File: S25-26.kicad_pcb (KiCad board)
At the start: 6 copper layers, 90 x 90 mm, 0 parts

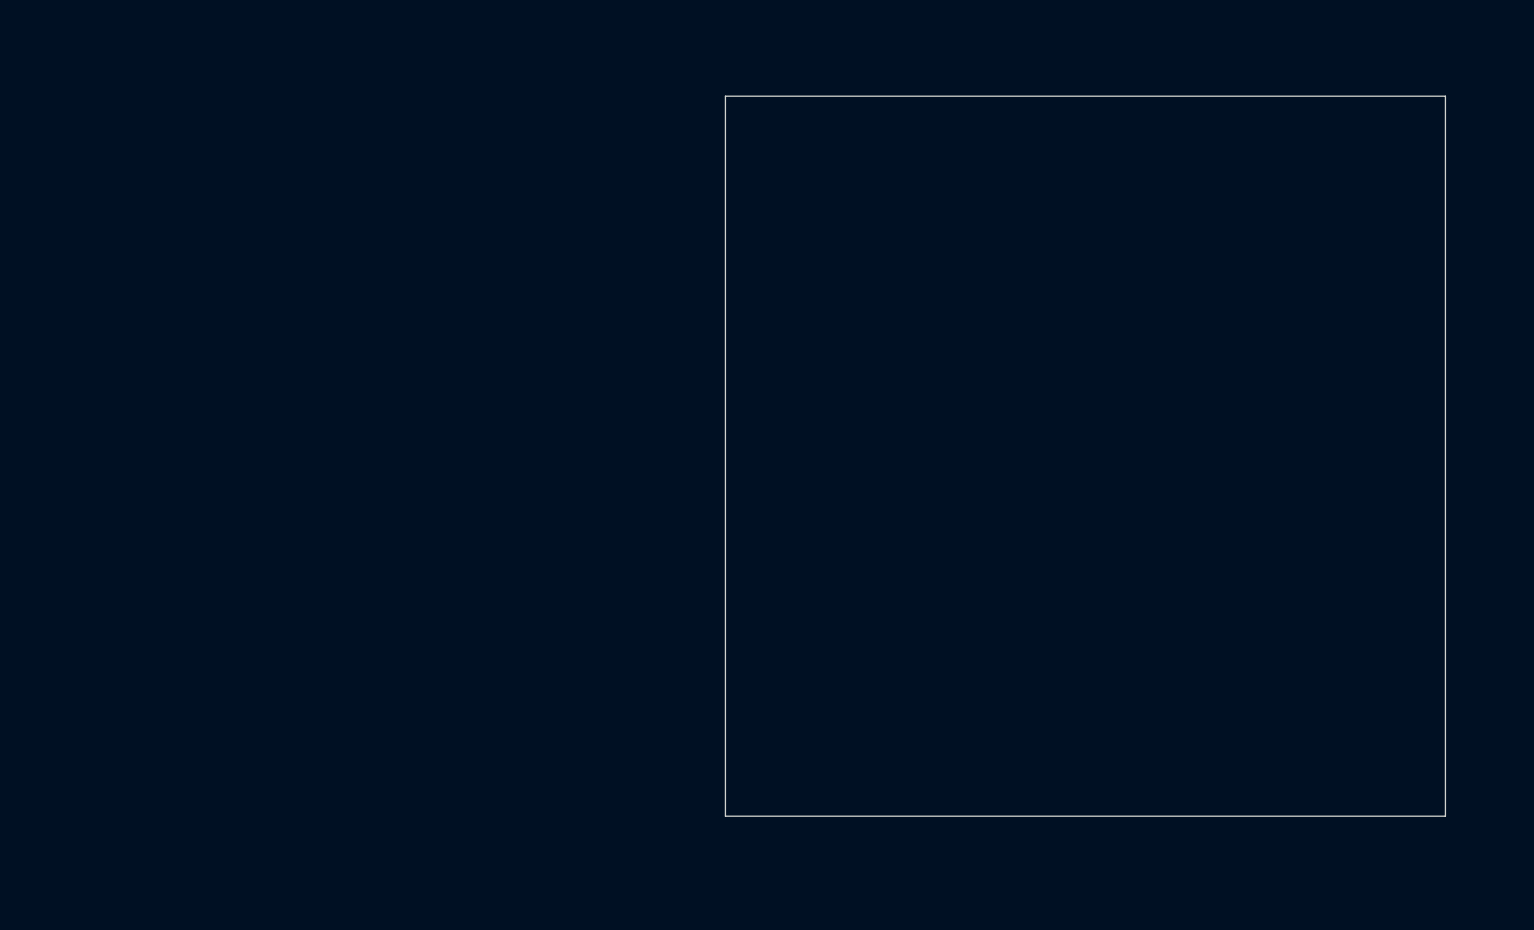
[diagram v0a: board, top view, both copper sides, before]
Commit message: 3v3 Regulator routed; zones for 3v3 and gnd
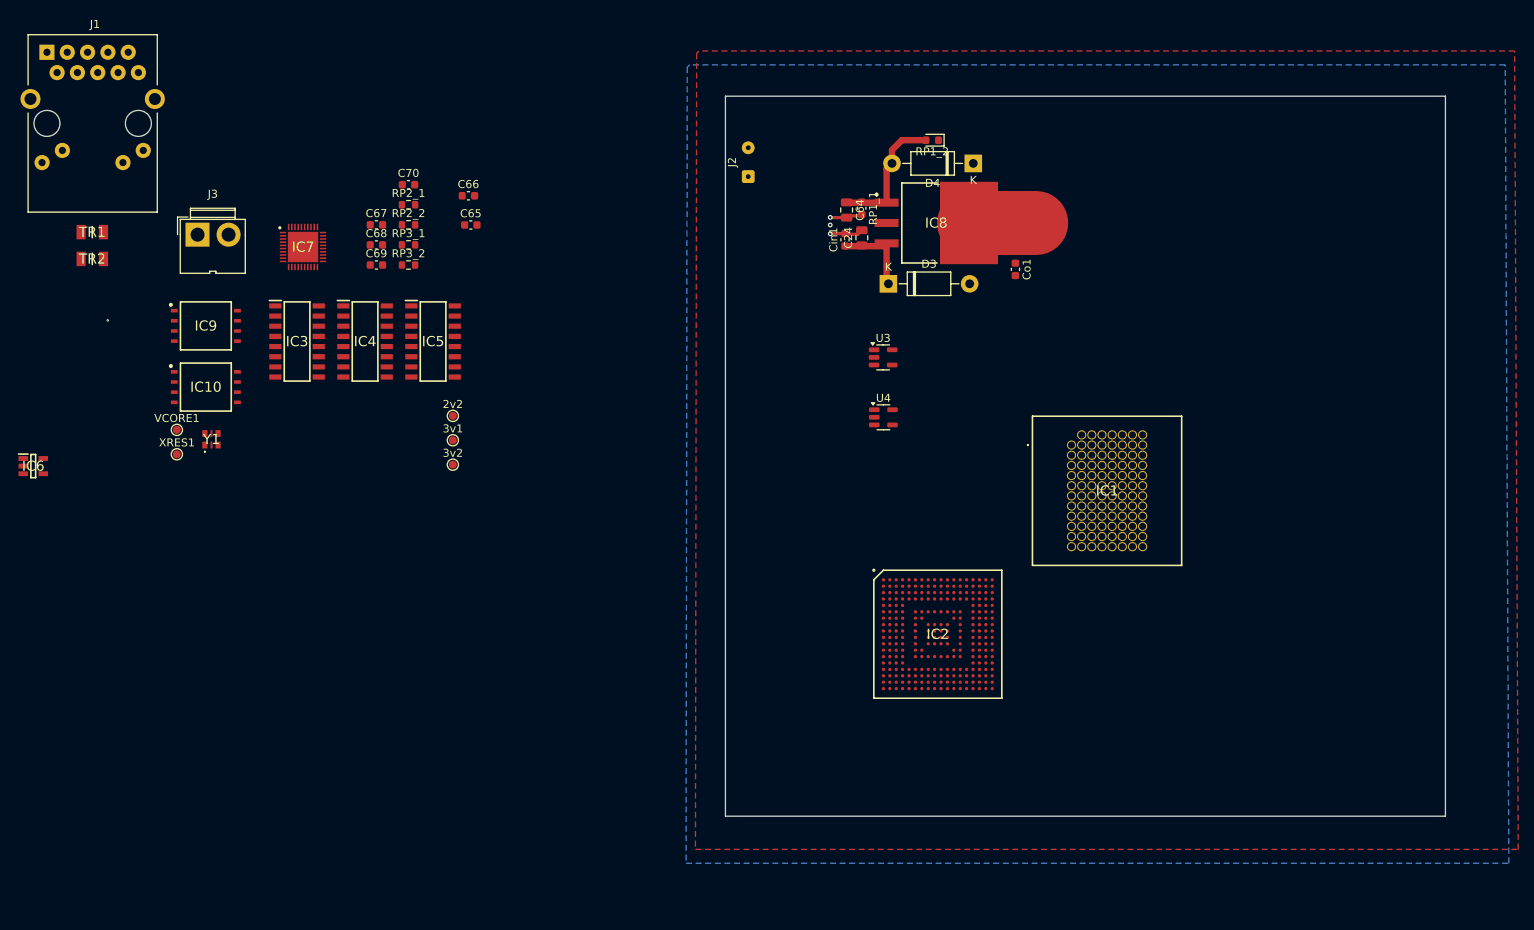
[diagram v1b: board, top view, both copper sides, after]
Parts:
- added 2v2: TestPoint, TestPoint:TestPoint_Pad_D1.0mm, F.Cu at (74.3, 90.2)
- added 3v1: TestPoint, TestPoint:TestPoint_Pad_D1.0mm, F.Cu at (74.3, 93.2)
- added 3v2: TestPoint, TestPoint:TestPoint_Pad_D1.0mm, F.Cu at (74.3, 96.3)
- added C24: 10uF, Capacitor_SMD:C_0805_2012Metric, F.Cu at (125.5, 67.9)
- added C64: 10uF, Capacitor_SMD:C_0805_2012Metric, F.Cu at (123.5, 64.4)
- added C65: 1uF, Capacitor_SMD:C_0603_1608Metric, F.Cu at (76.6, 66.3)
- added C66: 10nF, Capacitor_SMD:C_0603_1608Metric, F.Cu at (76.3, 62.6)
- added C67: 1uF, Capacitor_SMD:C_0603_1608Metric, F.Cu at (64.8, 66.3)
- added C68: 1uF, Capacitor_SMD:C_0603_1608Metric, F.Cu at (64.8, 68.8)
- added C69: 10nF, Capacitor_SMD:C_0603_1608Metric, F.Cu at (64.8, 71.3)
- added C70: 1uF, Capacitor_SMD:C_0603_1608Metric, F.Cu at (68.8, 61.3)
- added Cin1: 1uF, Capacitor_SMD:C_0603_1608Metric, F.Cu at (123.3, 68.2)
- added Co1: 1uF, Capacitor_SMD:C_0603_1608Metric, F.Cu at (144.7, 71.8)
- added D3: 1N4002, Diode_THT:D_DO-41_SOD81_P10.16mm_Horizontal, F.Cu at (128.8, 73.7)
- added D4: 1N4002, Diode_THT:D_DO-41_SOD81_P10.16mm_Horizontal, F.Cu at (139.4, 58.6)
- added IC1: CMV4000-3E5M0PN, SamacSys_Parts:CMV40003E5M0PN, F.Cu at (151.7, 93.8)
- added IC10: MT29F2G01ABAGDWB-IT_G_TR, SamacSys_Parts:SON127P800X600X65-8N, F.Cu at (43.5, 86.6)
- added IC2: XMC7200D-E272K8384AA, SamacSys_Parts:BGA272C80P18X18_1600X1600X170, F.Cu at (134.9, 117.5)
- added IC3: DS90LV048ATM_NOPB, SamacSys_Parts:SOIC127P600X175-16N, F.Cu at (54.9, 80.9)
- added IC4: DS90LV048ATM_NOPB, SamacSys_Parts:SOIC127P600X175-16N, F.Cu at (63.4, 80.9)
- added IC5: DS90LV048ATM_NOPB, SamacSys_Parts:SOIC127P600X175-16N, F.Cu at (71.9, 80.9)
- added IC6: DS90LV011AHMF_NOPB, SamacSys_Parts:SOT95P280X145-5N, F.Cu at (21.9, 96.4)
- added IC7: MXL86110I-AQB-R, SamacSys_Parts:QFN40P500X500X95-41N-D, F.Cu at (55.6, 69.0)
- added IC8: NCV317BD2TR4G, SamacSys_Parts:TO254P1420X457-4N, F.Cu at (134.8, 66.0)
- added IC9: MT29F2G01ABAGDWB-IT_G_TR, SamacSys_Parts:SON127P800X600X65-8N, F.Cu at (43.5, 78.9)
- added J1: RJ45_RB1-125B8G1A, Connector_RJ:RJ45_UDE_RB1-125B8G1A, F.Cu at (23.6, 44.7)
- added J2: DC_IN_PADS, Connector_Wire:SolderWire-0.1sqmm_1x02_P3.6mm_D0.4mm_OD1mm, F.Cu at (111.2, 60.2)
- added J3: Conn_01x02_Pin, Connector:JWT_A3963_1x02_P3.96mm_Vertical, F.Cu at (42.4, 67.5)
- added RP1_1: 164, Capacitor_SMD:C_0603_1608Metric, F.Cu at (125.5, 64.2)
- added RP1_2: 100, Diode_SMD:D_0603_1608Metric, F.Cu at (134.2, 55.7)
- added RP2_1: 100, Resistor_SMD:R_0603_1608Metric, F.Cu at (68.8, 63.8)
- added RP2_2: 150, Resistor_SMD:R_0603_1608Metric, F.Cu at (68.8, 66.3)
- added RP3_1: 120, Resistor_SMD:R_0603_1608Metric, F.Cu at (68.8, 68.8)
- added RP3_2: 90, Resistor_SMD:R_0603_1608Metric, F.Cu at (68.8, 71.3)
- added TR1: PTS120601B1K00P100, SamacSys_Parts:RESC3016X65N, F.Cu at (29.3, 67.2)
- added TR2: PTS120601B1K00P100, SamacSys_Parts:RESC3016X65N, F.Cu at (29.3, 70.5)
- added U3: TPS73601DBV, Package_TO_SOT_SMD:SOT-23-5, F.Cu at (128.1, 82.8)
- added U4: TPS73601DBV, Package_TO_SOT_SMD:SOT-23-5, F.Cu at (128.2, 90.3)
- added VCORE1: TestPoint, TestPoint:TestPoint_Pad_D1.0mm, F.Cu at (39.8, 91.9)
- added XRES1: TestPoint, TestPoint:TestPoint_Pad_D1.0mm, F.Cu at (39.8, 95.0)
- added Y1: DSC1101DM2-012.0000, SamacSys_Parts:DSC1101DM20120000, F.Cu at (44.2, 93.1)
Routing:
- net Net-(D4-A): track 0.00 -> 16.6 mm
- net /Voltage Regulation/DC_LINE_IN_28V: track 0.00 -> 11.0 mm
- net +3V3: track 0.00 -> 8.40 mm
- net GND: track 0.00 -> 8.32 mm, vias 0 -> 3
- net (no net): vias 0 -> 1
- added copper zone on F.Cu, net +3V3
- added copper zone on B.Cu, net GND
- added copper zone on In1.Cu, net GND
- added copper zone on In3.Cu, net GND

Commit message: Ethernet Transceiver
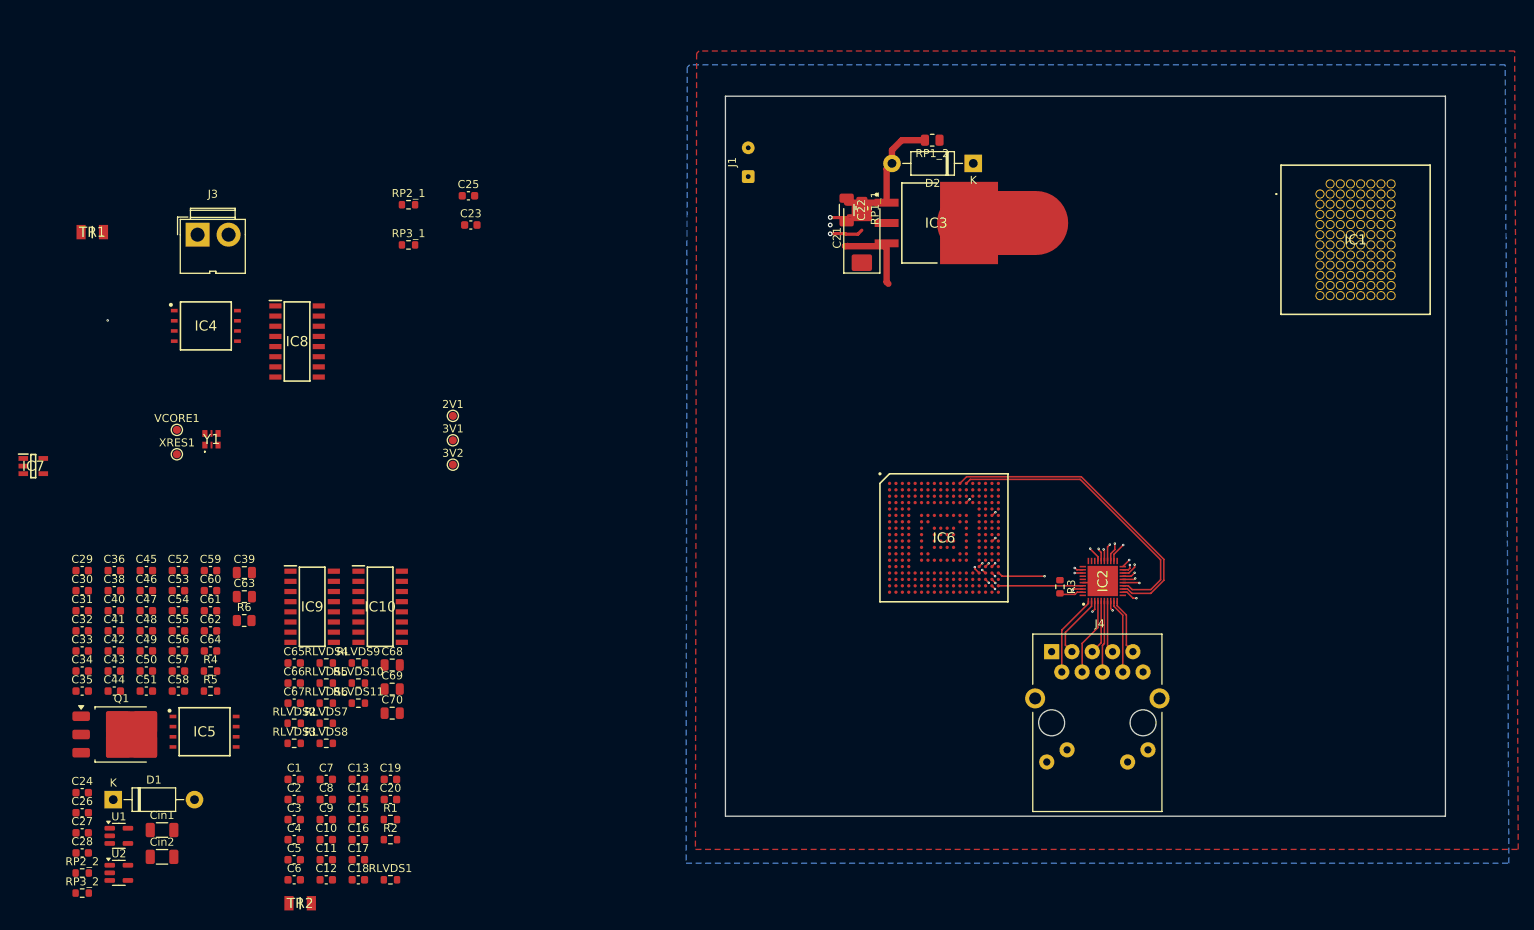
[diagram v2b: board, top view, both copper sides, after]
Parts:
- removed Co1: 1uF, Capacitor_SMD:C_0603_1608Metric
- removed D3: 1N4002, Diode_THT:D_DO-41_SOD81_P10.16mm_Horizontal
- removed the IC4 at (63.4, 80.9)
- removed U3, U4: TPS73601DBV, Package_TO_SOT_SMD:SOT-23-5
- added C1: 0.1uF, Capacitor_SMD:C_0603_1608Metric, F.Cu at (54.5, 135.6)
- added C10: 0.1uF, Capacitor_SMD:C_0603_1608Metric, F.Cu at (58.5, 143.1)
- added C11: 0.1uF, Capacitor_SMD:C_0603_1608Metric, F.Cu at (58.5, 145.6)
- added C12: 0.1uF, Capacitor_SMD:C_0603_1608Metric, F.Cu at (58.5, 148.2)
- added C13: 0.1uF, Capacitor_SMD:C_0603_1608Metric, F.Cu at (62.5, 135.6)
- added C14: 0.1uF, Capacitor_SMD:C_0603_1608Metric, F.Cu at (62.5, 138.1)
- added C15: 0.1uF, Capacitor_SMD:C_0603_1608Metric, F.Cu at (62.5, 140.6)
- added C16: 0.1uF, Capacitor_SMD:C_0603_1608Metric, F.Cu at (62.5, 143.1)
- added C17: 0.1uF, Capacitor_SMD:C_0603_1608Metric, F.Cu at (62.5, 145.6)
- added C18: 0.1uF, Capacitor_SMD:C_0603_1608Metric, F.Cu at (62.5, 148.2)
- added C19: 0.1uF, Capacitor_SMD:C_0603_1608Metric, F.Cu at (66.5, 135.6)
- added C2: 0.1uF, Capacitor_SMD:C_0603_1608Metric, F.Cu at (54.5, 138.1)
- added C20: 0.1uF, Capacitor_SMD:C_0603_1608Metric, F.Cu at (66.5, 138.1)
- added C24: 1uF, Capacitor_SMD:C_0603_1608Metric, F.Cu at (28.0, 137.3)
- added C26: 10nF, Capacitor_SMD:C_0603_1608Metric, F.Cu at (28.0, 139.8)
- added C27: 1uF, Capacitor_SMD:C_0603_1608Metric, F.Cu at (28.0, 142.3)
- added C28: 1uF, Capacitor_SMD:C_0603_1608Metric, F.Cu at (28.0, 144.8)
- added C29: 10uF, Capacitor_SMD:C_0603_1608Metric, F.Cu at (28.0, 109.5)
- added C3: 0.1uF, Capacitor_SMD:C_0603_1608Metric, F.Cu at (54.5, 140.6)
- added C30: 1uF, Capacitor_SMD:C_0603_1608Metric, F.Cu at (28.0, 112.0)
- added C31: 0.1uF, Capacitor_SMD:C_0603_1608Metric, F.Cu at (28.0, 114.5)
- added C32: 0.1uF, Capacitor_SMD:C_0603_1608Metric, F.Cu at (28.0, 117.0)
- added C33: 0.1uF, Capacitor_SMD:C_0603_1608Metric, F.Cu at (28.0, 119.5)
- added C34: 0.1uF, Capacitor_SMD:C_0603_1608Metric, F.Cu at (28.0, 122.0)
- added C35: 0.1uF, Capacitor_SMD:C_0603_1608Metric, F.Cu at (28.0, 124.6)
- added C36: 0.1uF, Capacitor_SMD:C_0603_1608Metric, F.Cu at (32.0, 109.5)
- added C38: 0.1uF, Capacitor_SMD:C_0603_1608Metric, F.Cu at (32.0, 112.0)
- added C39: 0.1uF, Capacitor_SMD:C_0805_2012Metric, F.Cu at (48.3, 109.8)
- added C4: 0.1uF, Capacitor_SMD:C_0603_1608Metric, F.Cu at (54.5, 143.1)
- added C40: 1uF, Capacitor_SMD:C_0603_1608Metric, F.Cu at (32.0, 114.5)
- added C41: 0.1uF, Capacitor_SMD:C_0603_1608Metric, F.Cu at (32.0, 117.0)
- added C42: 0.1uF, Capacitor_SMD:C_0603_1608Metric, F.Cu at (32.0, 119.5)
- added C43: 0.1uF, Capacitor_SMD:C_0603_1608Metric, F.Cu at (32.0, 122.0)
- added C44: 0.1uF, Capacitor_SMD:C_0603_1608Metric, F.Cu at (32.0, 124.6)
- added C45: 0.1uF, Capacitor_SMD:C_0603_1608Metric, F.Cu at (36.0, 109.5)
- added C46: 0.1uF, Capacitor_SMD:C_0603_1608Metric, F.Cu at (36.0, 112.0)
- added C47: 1uF, Capacitor_SMD:C_0603_1608Metric, F.Cu at (36.0, 114.5)
- added C48: 1uF, Capacitor_SMD:C_0603_1608Metric, F.Cu at (36.0, 117.0)
- added C49: 0.1uF, Capacitor_SMD:C_0603_1608Metric, F.Cu at (36.0, 119.5)
- added C5: 0.1uF, Capacitor_SMD:C_0603_1608Metric, F.Cu at (54.5, 145.6)
- added C50: 0.1uF, Capacitor_SMD:C_0603_1608Metric, F.Cu at (36.0, 122.0)
- added C51: 0.1uF, Capacitor_SMD:C_0603_1608Metric, F.Cu at (36.0, 124.6)
- added C52: 10nF, Capacitor_SMD:C_0603_1608Metric, F.Cu at (40.0, 109.5)
- added C53: 0.1uF, Capacitor_SMD:C_0603_1608Metric, F.Cu at (40.0, 112.0)
- added C54: 0.1uF, Capacitor_SMD:C_0603_1608Metric, F.Cu at (40.0, 114.5)
- added C55: 1uF, Capacitor_SMD:C_0603_1608Metric, F.Cu at (40.0, 117.0)
- added C56: 0.1uF, Capacitor_SMD:C_0603_1608Metric, F.Cu at (40.0, 119.5)
- added C57: 2.2uF, Capacitor_SMD:C_0603_1608Metric, F.Cu at (40.0, 122.0)
- added C58: 10nF, Capacitor_SMD:C_0603_1608Metric, F.Cu at (40.0, 124.6)
- added C59: 0.1uF, Capacitor_SMD:C_0603_1608Metric, F.Cu at (44.0, 109.5)
- added C6: 0.1uF, Capacitor_SMD:C_0603_1608Metric, F.Cu at (54.5, 148.2)
- added C60: 2.2uF, Capacitor_SMD:C_0603_1608Metric, F.Cu at (44.0, 112.0)
- added C61: 0.1uF, Capacitor_SMD:C_0603_1608Metric, F.Cu at (44.0, 114.5)
- added C62: 10uF, Capacitor_SMD:C_0603_1608Metric, F.Cu at (44.0, 117.0)
- added C63: 0.1uF, Capacitor_SMD:C_0805_2012Metric, F.Cu at (48.3, 112.8)
- added C64: 1nF, Capacitor_SMD:C_0603_1608Metric, F.Cu at (44.0, 119.5)
- added C65: 1nF, Capacitor_SMD:C_0603_1608Metric, F.Cu at (54.5, 121.0)
- added C66: 1nF, Capacitor_SMD:C_0603_1608Metric, F.Cu at (54.5, 123.6)
- added C7: 0.1uF, Capacitor_SMD:C_0603_1608Metric, F.Cu at (58.5, 135.6)
- added C8: 0.1uF, Capacitor_SMD:C_0603_1608Metric, F.Cu at (58.5, 138.1)
- added C9: 0.1uF, Capacitor_SMD:C_0603_1608Metric, F.Cu at (58.5, 140.6)
- added Cin2: 1uF, Capacitor_SMD:C_1206_3216Metric, F.Cu at (38.0, 145.3)
- added D1: 1N4002, Diode_THT:D_DO-41_SOD81_P10.16mm_Horizontal, F.Cu at (31.9, 138.1)
- added IC9: DS90LV048ATM_NOPB, SamacSys_Parts:SOIC127P600X175-16N, F.Cu at (56.7, 114.0)
- added Q1: ZXT849K, Package_TO_SOT_SMD:TO-252-3_TabPin4, F.Cu at (32.9, 130.0)
- added R1: 1k, Resistor_SMD:R_0603_1608Metric, F.Cu at (66.5, 140.6)
- added R2: 1k, Resistor_SMD:R_0603_1608Metric, F.Cu at (66.5, 143.1)
- added R3: 2.49k, Resistor_SMD:R_0603_1608Metric, F.Cu at (150.2, 111.5)
- added R4: 10k, Resistor_SMD:R_0603_1608Metric, F.Cu at (44.0, 122.0)
- added R5: 10k, Resistor_SMD:R_0603_1608Metric, F.Cu at (44.0, 124.6)
- added R6: 0.1, Resistor_SMD:R_0805_2012Metric, F.Cu at (48.2, 115.7)
- added RLVDS1: 100, Resistor_SMD:R_0603_1608Metric, F.Cu at (66.5, 148.2)
- added RLVDS10: 100, Resistor_SMD:R_0603_1608Metric, F.Cu at (62.5, 123.6)
- added RLVDS11: 100, Resistor_SMD:R_0603_1608Metric, F.Cu at (62.5, 126.1)
- added RLVDS2: 100, Resistor_SMD:R_0603_1608Metric, F.Cu at (54.5, 128.6)
- added RLVDS3: 100, Resistor_SMD:R_0603_1608Metric, F.Cu at (54.5, 131.1)
- added RLVDS4: 100, Resistor_SMD:R_0603_1608Metric, F.Cu at (58.5, 121.0)
- added RLVDS5: 100, Resistor_SMD:R_0603_1608Metric, F.Cu at (58.5, 123.6)
- added RLVDS6: 100, Resistor_SMD:R_0603_1608Metric, F.Cu at (58.5, 126.1)
- added RLVDS7: 100, Resistor_SMD:R_0603_1608Metric, F.Cu at (58.5, 128.6)
- added RLVDS8: 100, Resistor_SMD:R_0603_1608Metric, F.Cu at (58.5, 131.1)
- added RLVDS9: 100, Resistor_SMD:R_0603_1608Metric, F.Cu at (62.5, 121.0)
- added U1: TPS73601MDRBREP, Package_TO_SOT_SMD:SOT-23-5, F.Cu at (32.6, 142.7)
- added U2: TPS73601MDRBREP, Package_TO_SOT_SMD:SOT-23-5, F.Cu at (32.6, 147.3)
- C21: renamed from C24; footprint Capacitor_SMD:C_0805_2012Metric -> Capacitor_Tantalum_SMD:CP_EIA-7343-31_Kemet-D
- C22: renamed from C64; footprint Capacitor_SMD:C_0805_2012Metric -> Capacitor_SMD:C_1206_3216Metric
- C67: value 1uF -> 1nF
- C68, C70: value 1uF -> 0.1uF; footprint Capacitor_SMD:C_0603_1608Metric -> Capacitor_SMD:C_0805_2012Metric
- C69: value 10nF -> 0.1uF; footprint Capacitor_SMD:C_0603_1608Metric -> Capacitor_SMD:C_0805_2012Metric
- Cin1: footprint Capacitor_SMD:C_0603_1608Metric -> Capacitor_SMD:C_1206_3216Metric
- IC10: value MT29F2G01ABAGDWB-IT_G_TR -> DS90LV048ATM_NOPB; footprint SamacSys_Parts:SON127P800X600X65-8N -> SamacSys_Parts:SOIC127P600X175-16N
- IC5: value DS90LV048ATM_NOPB -> MT29F2G01ABAGDWB-IT_G_TR; footprint SamacSys_Parts:SOIC127P600X175-16N -> SamacSys_Parts:SON127P800X600X65-8N
- RP1_1: value 164 -> 165; footprint Capacitor_SMD:C_0603_1608Metric -> Resistor_SMD:R_0805_2012Metric
- RP1_2: footprint Diode_SMD:D_0603_1608Metric -> Resistor_SMD:R_0805_2012Metric
- RP2_1: value 100 -> 46.4k
- RP2_2: value 150 -> 30.9k
- RP3_1: value 120 -> 31.6k
- RP3_2: value 90 -> 42.2k
- moved J4 146.2 mm to (149.2, 119.6)
- moved Cin1 112.8 mm to (38.0, 141.9), turned to 0 degrees
- moved IC2 108.3 mm to (155.6, 110.8), turned to 90 degrees
- moved RP2_2 90.7 mm to (28.0, 147.3)
- moved RP3_2 88.5 mm to (28.0, 149.8)
- moved TR2 84.6 mm to (55.2, 151.1)
- moved C70 66.1 mm to (66.7, 127.3)
- moved C67 60.7 mm to (54.5, 126.1)
- moved IC5 56.5 mm to (43.3, 129.6)
- moved C69 53.0 mm to (66.7, 124.3)
- moved C68 52.5 mm to (66.7, 121.3)
- moved IC1 44.2 mm to (182.7, 62.4)
- moved IC10 35.1 mm to (65.2, 114.0)
- moved IC6 12.1 mm to (135.7, 105.4)
- renumbered 2v2 to 2V1, 3v1 to 3V1, 3v2 to 3V2, C65 to C23, C66 to C25, D4 to D2, IC7 to IC2, IC8 to IC3, IC9 to IC4, IC2 to IC6, IC6 to IC7, IC3 to IC8, J2 to J1, J1 to J4
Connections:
- net /BI_DN_P renamed /BI_DB_N
- C67 pad 1: +3V -> +3V3
- C69 pad 1: +2V1 -> +3V3
- C69 pad 2: Net-(U4-FB) -> GND
- C70 pad 1: +2V1 -> +3V3
- IC10 pad 1: /Processing/SCB2_SEL0 -> /LVDS Conversion/LVDS_CLK_OUT_N
- IC10 pad 2: /Processing/SCB2_MISO -> /LVDS Conversion/LVDS_CLK_OUT_P
- IC10 pad 4: GND -> unconnected-(IC10-RIN2--Pad4)
- IC10 pad 5: /Processing/SCB2_MOSI -> unconnected-(IC10-RIN3--Pad5)
- IC10 pad 6: /Processing/SCB2_CLK -> unconnected-(IC10-RIN3+-Pad6)
- IC10 pad 7: unconnected-(IC10-HOLD#/IO3-Pad7) -> /LVDS Conversion/LVDS_CTR_OUT_P
- IC10 pad 8: +3V3 -> /LVDS Conversion/LVDS_CTR_OUT_N
- IC2 pad 12: unconnected-(IC7-HRSTN-Pad12) -> /HRSTN
- IC2 pad 36: unconnected-(IC7-XTAL1-Pad36) -> GND
- IC2 pad 37: unconnected-(IC7-XTAL2/CLK-Pad37) -> /ETH0_REF_CLK
- IC4 pad 1: /Processing/SCB0_SEL0 -> /Processing/QSPI_SEL0
- IC4 pad 2: /Processing/SCB0_MISO -> /Processing/QSPI_IO1
- IC4 pad 3: unconnected-(IC9-WP#/IO2-Pad3) -> /Processing/QSPI_IO2
- IC4 pad 5: /Processing/SCB0_MOSI -> /Processing/QSPI_IO0
- IC4 pad 6: /Processing/SCB0_CLK -> /Processing/QSPI_SCLK
- IC4 pad 7: unconnected-(IC9-HOLD#/IO3-Pad7) -> /Processing/QSPI_IO3
- IC5 pad 1: /LVDS Conversion/LVDS_CLK_OUT_N -> /Processing/QSPI_SEL1
- IC5 pad 2: /LVDS Conversion/LVDS_CLK_OUT_P -> /Processing/QSPI_IO1
- IC5 pad 3: unconnected-(IC5-RIN2+-Pad3) -> /Processing/QSPI_IO2
- IC5 pad 4: unconnected-(IC5-RIN2--Pad4) -> GND
- IC5 pad 5: unconnected-(IC5-RIN3--Pad5) -> /Processing/QSPI_IO0
- IC5 pad 6: unconnected-(IC5-RIN3+-Pad6) -> /Processing/QSPI_SCLK
- IC5 pad 7: /LVDS Conversion/LVDS_CTR_OUT_P -> /Processing/QSPI_IO3
- IC5 pad 8: /LVDS Conversion/LVDS_CTR_OUT_N -> +3V3
- IC6 pad C11: unconnected-(IC2B-P3.6-PadC11) -> /CMOS_RESET_N
- IC6 pad C14: /Processing/ETH0_RX_ER (P2.2) -> unconnected-(IC6B-P2.2-PadC14)
- IC6 pad D11: unconnected-(IC2B-P3.7-PadD11) -> /FRAME_REQ
- IC6 pad D13: unconnected-(IC2B-P2.6-PadD13) -> /HRSTN
- IC6 pad D14: /Processing/ETH0_ETH_TSU_TIMER_CMP_VAL (P2.3) -> unconnected-(IC6B-P2.3-PadD14)
- IC6 pad D5: unconnected-(IC2B-P5.5-PadD5) -> /LVDS Conversion/LVDS_RECV_EN
- IC6 pad J3: unconnected-(IC2B-P24.0-PadJ3) -> /LVDS Conversion/CMOS_CLK_OUT
- IC6 pad J4: unconnected-(IC2B-P24.1-PadJ4) -> /Processing/QSPI_CLK
- IC6 pad K2: unconnected-(IC2B-P24.3-PadK2) -> /Processing/QSPI_SEL0
- IC6 pad K3: unconnected-(IC2B-P24.4-PadK3) -> /Processing/QSPI_SEL1
- IC6 pad K4: unconnected-(IC2B-P25.0-PadK4) -> /Processing/QSPI_IO0
- IC6 pad L1: unconnected-(IC2B-P25.1-PadL1) -> /Processing/QSPI_IO1
- IC6 pad L2: unconnected-(IC2B-P25.2-PadL2) -> /Processing/QSPI_IO2
- IC6 pad L3: unconnected-(IC2B-P25.3-PadL3) -> /Processing/QSPI_IO3
- IC6 pad T18: /Processing/ETH0_TX_ER (P18.2) -> unconnected-(IC6B-P18.2-PadT18)
- IC6 pad U18: /Processing/ETH0_REF_CLK (P18.0) -> /ETH0_REF_CLK
- RP3_1 pad 2: Net-(U4-FB) -> Net-(U2-FB)
- RP3_2 pad 1: Net-(U4-FB) -> Net-(U2-FB)
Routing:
- net /ETH0_MDC: track 0.00 -> 38.8 mm
- net /ETH0_MDIO: track 0.00 -> 36.6 mm
- net /HRSTN: track 0.00 -> 33.3 mm, vias 0 -> 2
- net /PHY_LED0: track 0.00 -> 29.7 mm, vias 0 -> 1
- net /ETH0_RXD_3: track 0.00 -> 27.4 mm, vias 0 -> 2
- net /ETH0_TXD_2: track 0.00 -> 27.1 mm, vias 0 -> 2
- net /ETH0_RXD_2: track 0.00 -> 25.4 mm, vias 0 -> 2
- net /ETH0_TXD_3: track 0.00 -> 22.2 mm, vias 0 -> 2
- net /ETH0_TXD_0: track 0.00 -> 21.3 mm, vias 0 -> 2
- net /ETH0_RX_CLK: track 0.00 -> 21.0 mm, vias 0 -> 2
- net /ETH0_RX_CTL: track 0.00 -> 20.7 mm, vias 0 -> 2
- net /ETH0_RXD_1: track 0.00 -> 20.2 mm, vias 0 -> 2
- net /ETH0_RXD_0: track 0.00 -> 20.1 mm, vias 0 -> 2
- net /ETH0_TXD_1: track 0.00 -> 20.0 mm, vias 0 -> 2
- net /ETH0_TX_CTL: track 0.00 -> 19.2 mm, vias 0 -> 2
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
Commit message: Memory layout completed
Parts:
- moved C43 91.7 mm to (122.1, 105.1), turned to 90 degrees
- moved C42 90.9 mm to (122.6, 112.4), turned to 90 degrees
- moved IC4 81.7 mm to (116.7, 115.2)
- moved IC5 76.5 mm to (116.7, 108.0)
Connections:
- IC6 pad J4: /Processing/QSPI_CLK -> /Processing/QSPI_SCLK
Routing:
- net /Processing/QSPI_IO0: track 0.00 -> 31.3 mm, vias 0 -> 3
- net /PHY_LED0: track 29.7 -> 60.4 mm
- net /Processing/QSPI_SCLK: track 0.00 -> 28.9 mm, vias 0 -> 3
- net /Processing/QSPI_IO2: track 0.00 -> 27.2 mm, vias 0 -> 3
- net /Processing/QSPI_IO1: track 0.00 -> 25.1 mm
- net /Processing/QSPI_IO3: track 0.00 -> 24.2 mm, vias 0 -> 3
- net /Processing/QSPI_SEL0: track 0.00 -> 20.4 mm, vias 0 -> 2
- net /VDD1V1: track 4.04 -> 23.8 mm, vias 3 -> 5
- net /Processing/QSPI_SEL1: track 0.00 -> 18.6 mm, vias 0 -> 2
- net GND: track 10.9 -> 19.9 mm, vias 3 -> 35
- net +3V3: track 8.40 -> 11.9 mm
- net /PHY_LED1: track 1.01 -> 0.00 mm, vias 1 -> 0
